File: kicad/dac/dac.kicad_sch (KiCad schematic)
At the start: 69 parts, among them J2 AudioJack3_SwitchT, J3 AudioJack3_SwitchTR, J3 Conn_01x09_Pin, J4 AudioJack3, K1 Relay, Q1 NPN, Q2 PNP, Q3 PNP, Q4 PNP, Q5 PNP, Q6 PNP, Q7 PNP, U1 PCM510xA

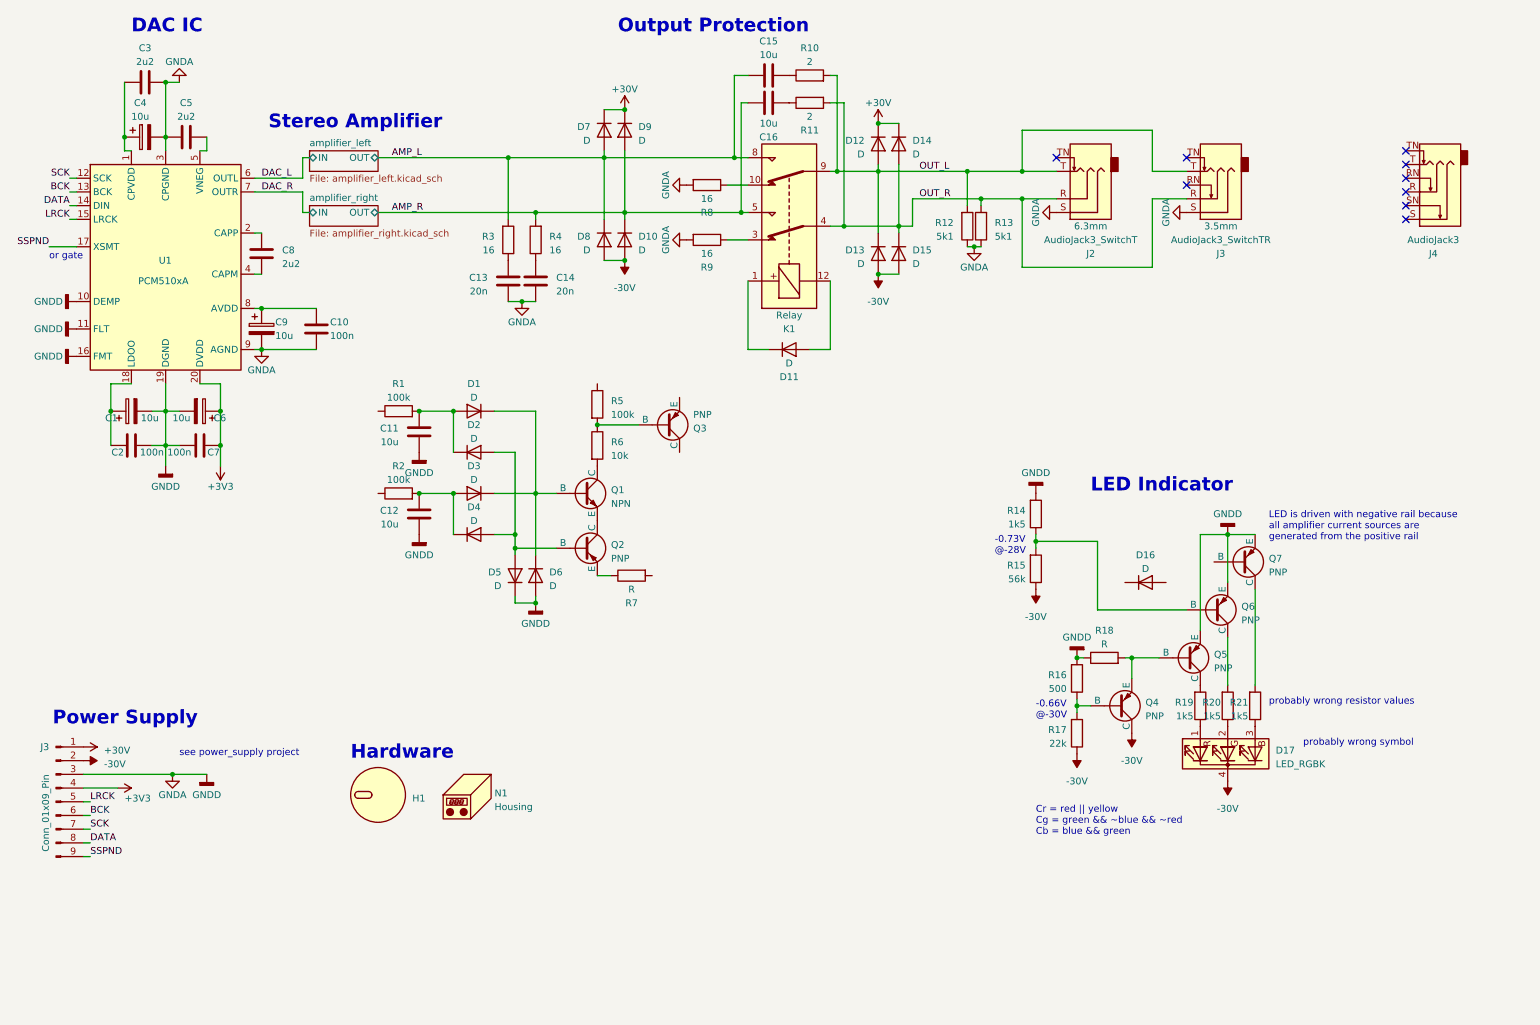
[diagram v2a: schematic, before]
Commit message: completed power supply footprints and placement
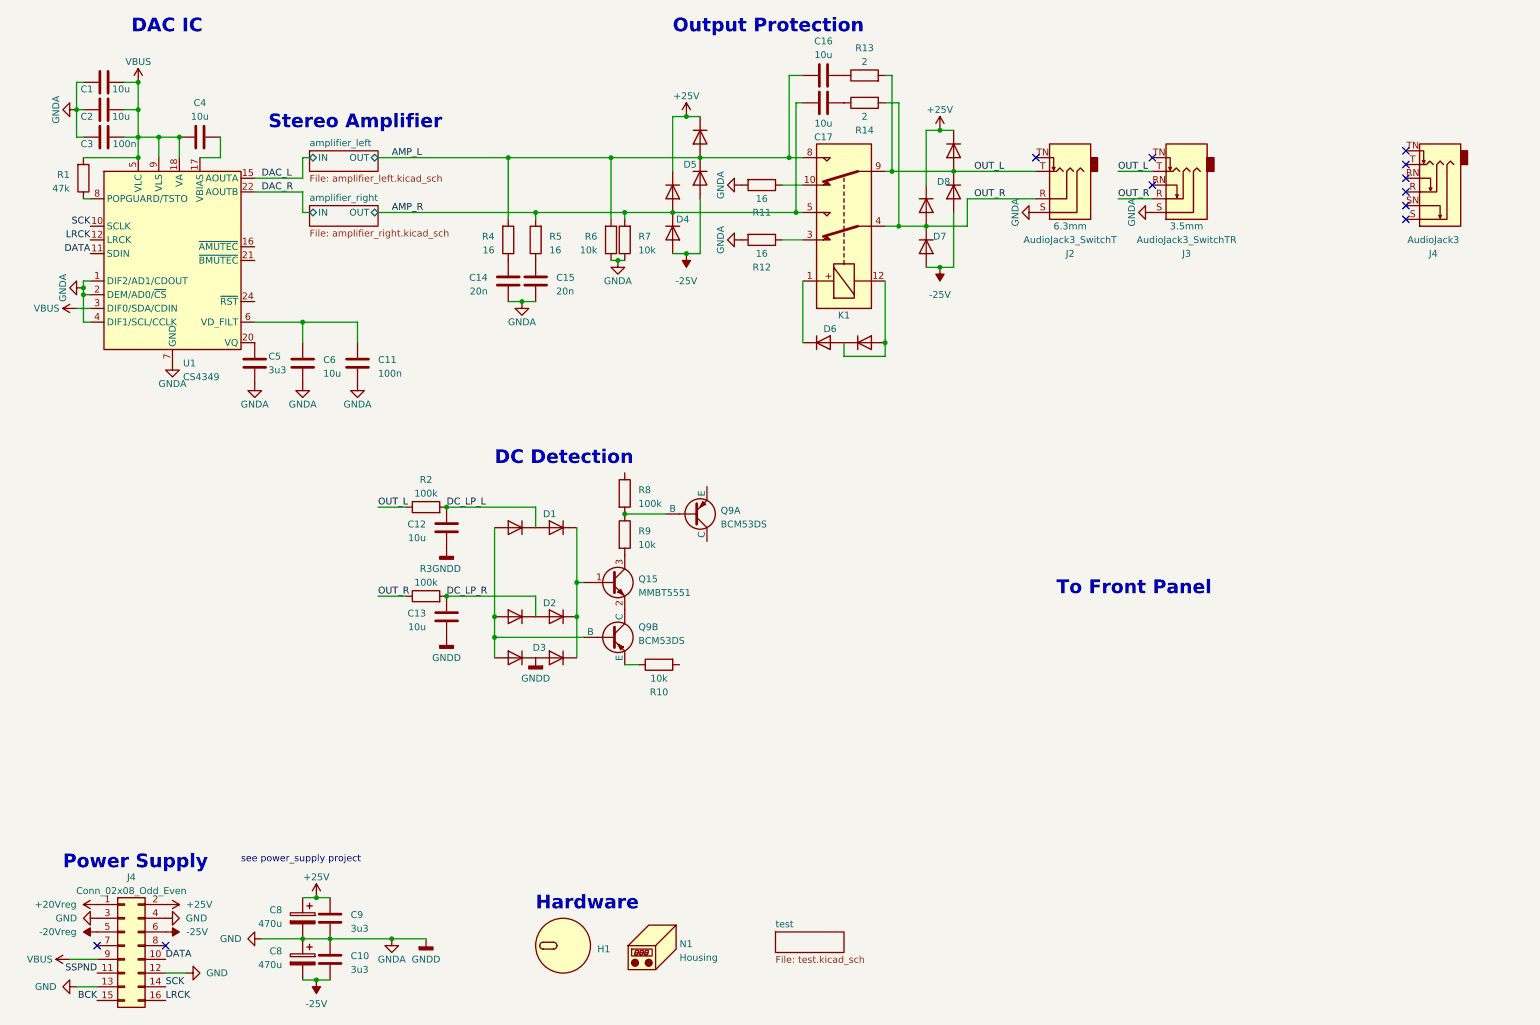
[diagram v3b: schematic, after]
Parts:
- removed C1, C4, C6, C9: 10u, symbol Device:C_Polarized
- removed C12: 10u, symbol Device:C
- removed C15: 10u, Capacitor_SMD:C_1206_3216Metric_Pad1.33x1.80mm_HandSolder, symbol Device:C
- removed C7: 100n, Capacitor_SMD:C_1206_3216Metric_Pad1.33x1.80mm_HandSolder, symbol Device:C
- removed C8: 2u2, Capacitor_SMD:C_1206_3216Metric_Pad1.33x1.80mm_HandSolder, symbol Device:C
- removed D1, D10, D11, D12, D13, D14, D15, D16, D2, D3, D4, D5, D6, D7, D8, D9: D, symbol Device:D
- removed D17: LED_RGBK, symbol Device:LED_RGBK
- removed J3: Conn_01x09_Pin, Connector_PinHeader_2.54mm:PinHeader_1x09_P2.54mm_Vertical, symbol Connector:Conn_01x09_Pin
- removed Q1: NPN, symbol Simulation_SPICE:NPN
- removed Q2, Q3: PNP, symbol Simulation_SPICE:PNP
- removed Q4, Q5, Q6, Q7: PNP, Package_TO_SOT_THT:TO-92, symbol Simulation_SPICE:PNP
- removed R14, R19, R20, R21: 1k5, Resistor_SMD:R_1206_3216Metric_Pad1.30x1.75mm_HandSolder, symbol Device:R
- removed R15: 56k, Resistor_SMD:R_1206_3216Metric_Pad1.30x1.75mm_HandSolder, symbol Device:R
- removed R16: 500, Resistor_SMD:R_1206_3216Metric_Pad1.30x1.75mm_HandSolder, symbol Device:R
- removed R17: 22k, Resistor_SMD:R_1206_3216Metric_Pad1.30x1.75mm_HandSolder, symbol Device:R
- removed R18: R, Resistor_SMD:R_1206_3216Metric_Pad1.30x1.75mm_HandSolder, symbol Device:R
- removed U1: PCM510xA, Package_SO:TSSOP-20_4.4x6.5mm_P0.65mm, symbol library:PCM510xA
- added C1, C13, C17, C4, C6: 10u, Capacitor_SMD:C_1206_3216Metric_Pad1.33x1.80mm_HandSolder, symbol Device:C
- added C11: 100n, Capacitor_SMD:C_1206_3216Metric_Pad1.33x1.80mm_HandSolder, symbol Device:C
- added C8 (x2): 470u, Capacitor_THT:CP_Radial_D10.0mm_P5.00mm, symbol Device:C_Polarized
- added C9: 3u3, Capacitor_THT:C_Rect_L7.2mm_W7.2mm_P5.00mm_FKS2_FKP2_MKS2_MKP2, symbol Device:C
- added D1, D2, D3, D4, D5, D6, D7, D8: ~, Package_TO_SOT_SMD:SOT-23-3, symbol library:Dual_Diode_Array
- added J4: Conn_02x08_Odd_Even, Connector_PinSocket_2.54mm:PinSocket_2x08_P2.54mm_Vertical, symbol Connector_Generic:Conn_02x08_Odd_Even
- added Q15: MMBT5551, Package_TO_SOT_SMD:SOT-23-3, symbol Device:Q_NPN_BEC
- added Q9: BCM53DS, Package_SO:SC-74-6_1.5x2.9mm_P0.95mm, symbol library:Dual-PNP
- added R1: 47k, Resistor_SMD:R_1206_3216Metric_Pad1.30x1.75mm_HandSolder, symbol Device:R
- added U1: CS4349, Package_SO:TSSOP-24_4.4x7.8mm_P0.65mm, symbol library:CS4349
- C10: value 100n -> 3u3; footprint Capacitor_SMD:C_1206_3216Metric_Pad1.33x1.80mm_HandSolder -> Capacitor_THT:C_Rect_L7.2mm_W7.2mm_P5.00mm_FKS2_FKP2_MKS2_MKP2; Digikey (none) -> 1928-1645-ND; Height (none) -> 13mm
- C12: renamed from C11; footprint (none) -> Capacitor_SMD:C_1206_3216Metric_Pad1.33x1.80mm_HandSolder; Digikey (none) -> 1276-3100-1-ND
- C16: Digikey (none) -> 1276-3100-1-ND
- C2: value 100n -> 10u; Digikey (none) -> 1276-3100-1-ND
- C3: value 2u2 -> 100n
- C5: value 2u2 -> 3u3
- R10: renamed from R7; value R -> 10k; footprint (none) -> Resistor_SMD:R_1206_3216Metric_Pad1.30x1.75mm_HandSolder
- R2: renamed from R1; footprint (none) -> Resistor_SMD:R_1206_3216Metric_Pad1.30x1.75mm_HandSolder
- R3: renamed from R2; footprint (none) -> Resistor_SMD:R_1206_3216Metric_Pad1.30x1.75mm_HandSolder
- R6: renamed from R12; value 5k1 -> 10k
- R7: renamed from R13; value 5k1 -> 10k
- R8: renamed from R5; footprint (none) -> Resistor_SMD:R_1206_3216Metric_Pad1.30x1.75mm_HandSolder
- R9: renamed from R6; footprint (none) -> Resistor_SMD:R_1206_3216Metric_Pad1.30x1.75mm_HandSolder
- renumbered C13 to C14, C14 to C15, R8 to R11, R9 to R12, R10 to R13, R11 to R14, R3 to R4, R4 to R5
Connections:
- net AMP_L: now also C16.1, R6.2, D5.3 (C/A)
- net AMP_R: now also R7.2, C17.1, D4.3 (C/A); no longer C16.1
- net BCK: now also J4.15 (Pin_15)
- net DAC_L: now also U1.15 (AOUTA)
- net DAC_R: now also U1.22 (AOUTB)
- net DATA: now also J4.10 (Pin_10), U1.11 (SDIN)
- net LRCK: now also J4.16 (Pin_16), U1.12 (LRCK)
- net OUT_L: now also R2.1, D8.3 (C/A); no longer R6.2
- net OUT_R: now also R3.1, D7.3 (C/A); no longer R7.2
- net SCK: now also J4.14 (Pin_14), U1.10 (SCLK)
- net SSPND: now also J4.11 (Pin_11)
- net -25V: now reaches C10.1
- net -25V: now also C8.2, D4.1 (A), D5.1 (A), D7.1 (A), D8.1 (A), J4.6 (Pin_6)
- net DC_LP_L: now reaches C12.1, R2.2
- net DC_LP_L: now also D1.3 (C/A)
- net at R9.2: now also Q15.3 (C)
- net at R8.2, R9.1: now also Q9.1 (B)
- net at R10.1: now also Q9.4 (E)
- net VBUS: now reaches C3.1
- net VBUS: now also C2.2, C1.2, C4.1, J4.9 (Pin_9), R1.2, U1.18 (VA), U1.3 (DIF0/SDA/CDIN), U1.5 (VLC), U1.9 (VLS)
- net at K1.1: now also D6.2 (C)
- net at K1.12: now also D6.1 (A), D6.3 (C/A)
- net at R14.1: now also C17.2; no longer C16.2
- net GND: now reaches C5.2
- net GND: now also C10.2, C12.2, C14.1, C15.1, C2.1, C3.2, J2.S, J3.S, R11.2, R12.2, R6.1, R7.1, C1.1, C11.2, C13.2, C6.2, C8.1, C8.2, C9.1, D3.3 (C/A), J4.12 (Pin_12), J4.13 (Pin_13), J4.3 (Pin_3), J4.4 (Pin_4), U1.1 (DIF2/AD1/CDOUT), U1.19 (GND), U1.2 (DEM/AD0/~{CS}), U1.4 (DIF1/SCL/CCLK), U1.7 (GND)
- net DC_LP_R: now reaches R3.2
- net DC_LP_R: now also C13.1, D2.3 (C/A)
- net at R13.1: now also C16.2
- removed net GNDA: C10.2, C12.2, C14.1, C15.1, C2.1, C3.2, C5.1, J2.S, J3.S, R11.2, R12.2, R6.1, R7.1
- new net: C4.2, U1.17 (VBIAS)
- new net: C5.1, U1.20 (VQ)
- new net: C11.1, C6.1, U1.6 (VD_FILT)
- new net: R1.1, U1.8 (POPGUARD/TSTO)
- new net: D1.2 (C), D2.2 (C), D3.2 (C), Q15.1 (B)
- new net: Q15.2 (E), Q9.3 (C)
- new net: D1.1 (A), D2.1 (A), D3.1 (A), Q9.2 (B)
- new net +20Vreg: J4.1 (Pin_1)
- new net +25V: C8.1, C9.2, D4.2 (C), D5.2 (C), D7.2 (C), D8.2 (C), J4.2 (Pin_2)
- new net -20Vreg: J4.5 (Pin_5)
- no-connect marks 9 -> 11
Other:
- added sheet test (test.kicad_sch)
- note added: "DC Detection"
- note added: "To Front Panel"
- note removed: "-0.66V @-30V"
- note removed: "-0.73V @-28V"
- note removed: "Cr = red || yellow Cg = green && ~blue && ~red Cb = blue && green"
- note removed: "LED Indicator"
- note removed: "LED is driven with negative rail because all amplifier current sources are generated from the positive rail"
- note removed: "or gate"
- note removed: "probably wrong resistor values"
- note removed: "probably wrong symbol"
- company: (none) -> Author: Jona Heinke
- title: USB DAC & Headphone Amplifier -> DAC & Headphone Amplifier
- moved on the sheet: C12, H1, J2, J3, K1, N1, R10, R11, R12, R13, R14, R2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

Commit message: commit
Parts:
- removed C14, C15: 20n, Capacitor_SMD:C_1206_3216Metric_Pad1.33x1.80mm_HandSolder, symbol Device:C
- removed D1, D2, D3, D4, D5, D6, D7, D8: ~, Package_TO_SOT_SMD:SOT-23-3, symbol library:Dual_Diode_Array
- removed R11, R12, R4, R5: 16, Resistor_SMD:R_1206_3216Metric_Pad1.30x1.75mm_HandSolder, symbol Device:R
- added D7: D, Diode_SMD:D_SOD-323_HandSoldering, symbol Device:D
- added D9 (x5): ~, Package_TO_SOT_SMD:SOT-23-3, symbol Device:D_Dual_Series_ACK
- added J5: Conn_01x06, symbol Connector_Generic:Conn_01x06
- added R6, R7: 16, Resistor_SMD:R_1206_3216Metric_Pad1.30x1.75mm_HandSolder, symbol Device:R
- J3: renamed from J4; now not fitted; now left out of the parts list
- K1: footprint (none) -> Relay_SMD:Relay_DPDT_Omron_G6K-2F-Y
- renumbered C11 to C10, C6 to C11, C16 to C12, C17 to C13, C12 to C14, C13 to C15, C5 to C7, C9 to C8, C10 to C9, J3 to J4, R8 to R10, R9 to R11, R10 to R12, R6 to R2, R7 to R3, R2 to R4, R3 to R5, R13 to R8, R14 to R9
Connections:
- net +25V: now also D9.3 (K), D9.3 (K), J5.1 (Pin_1)
- net -25V: now also D9.1 (A), D9.1 (A), J5.2 (Pin_2)
- net DC_LP_L: now also D9.2 (common)
- net DC_LP_R: now also D9.2 (common)
- net GND: now also C1.2, C2.2, D9.2 (common), J5.3 (Pin_3), R6.1, R7.1; no longer C1.1, C2.1
- net OUT_L: now also D9.2 (common)
- net OUT_R: now also D9.2 (common)
- net VBUS: now also C1.1, C2.1, R1.1; no longer C1.2, C2.2, R1.2
- net VBIAS: now reaches C4.2, U1.17 (VBIAS)
- net VQ: now reaches C7.1, U1.20 (VQ)
- net VD_FILT: now reaches C10.1, C11.1, U1.6 (VD_FILT)
- net POPGUARD: now reaches U1.8 (POPGUARD/TSTO)
- net POPGUARD: now also R1.2; no longer R1.1
- net at Q15.1 (B): now also D9.3 (K), D9.3 (K), D9.3 (K)
- net PROT_ARC_R: now reaches C13.2, R9.1
- net RLY+: now reaches K1.1
- net RLY+: now also D7.1 (K)
- net RLY_NC_L: now reaches K1.10
- net RLY_NC_L: now also R6.2
- net RLY-: now reaches K1.12
- net RLY-: now also D7.2 (A)
- net RLY_NC_R: now reaches K1.3
- net RLY_NC_R: now also R7.2
- net at Q9.2 (B): now also D9.1 (A), D9.1 (A), D9.1 (A)
- net PROT_ARC_L: now reaches C12.2, R8.1
- no-connect marks 11 -> 14
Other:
- note added: "DC USB"
- note added: "Input Pin Header From Power Supply Board"
- note added: "Output Jacks"
- note added: "fix relay pinout"
- note removed: "Power Supply"
- moved on the sheet: C11, C12, C13, C14, C15, C4, C7, J2, J4, K1, Q15, Q9A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

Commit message: commit
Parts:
- removed D9 (x3): ~, Package_TO_SOT_SMD:SOT-23-3, symbol Device:D_Dual_Series_ACK
- removed J3: AudioJack3, symbol Connector_Audio:AudioJack3_Switch
- removed Q15: MMBT5551, Package_TO_SOT_SMD:SOT-23-3, symbol Device:Q_NPN_BEC
- removed Q9: BCM53DS, Package_SO:SC-74-6_1.5x2.9mm_P0.95mm, symbol library:Dual-PNP
- removed R12: 10k, Resistor_SMD:R_1206_3216Metric_Pad1.30x1.75mm_HandSolder, symbol Device:R
- added C14: 3u3, Capacitor_SMD:C_1206_3216Metric_Pad1.33x1.80mm_HandSolder, symbol Device:C
- added D4, D5: TVS, Diode_SMD:D_SMB_Handsoldering, symbol Device:D_TVS
- added Q4: BCM53DS, Package_SO:SC-74-6_1.5x2.9mm_P0.95mm, symbol library:Dual-PNP
- added Q6: BCM56DS, Package_SO:SC-74-6_1.5x2.9mm_P0.95mm, symbol library:Dual-NPN
- added R4, R5, R8: 27k, Resistor_SMD:R_1206_3216Metric_Pad1.30x1.75mm_HandSolder, symbol Device:R
- added R6, R7: 47k, Resistor_SMD:R_1206_3216Metric_Pad1.30x1.75mm_HandSolder, symbol Device:R
- renumbered C4 to C10, C7 to C11, C10 to C12, C11 to C13, C12 to C15, C13 to C16, C8 to C3, C9 to C4, C1 to C5, C2 to C6, C3 to C7, C14 to C8, C15 to C9, J5 to J2, J4 to J3, J2 to J4, R3 to R10, R10 to R11, R11 to R12, R6 to R13, R7 to R14, R8 to R15, R9 to R16, R4 to R2, R5 to R3, R2 to R9
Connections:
- net RLY- is gone; now on net GND: D7.2 (A), K1.12
- net +25V: now also R11.1, C14.1, Q4.4 (E2), R8.1
- net AMP_L: now also R2.1
- net AMP_R: now also R3.1
- net DC_LP_L: now also R4.1; no longer D9.2 (common)
- net DC_LP_R: now also R5.1; no longer D9.2 (common)
- net GND: now also D4.1 (A1), D5.1 (A1), Q4.6 (C1), Q6.4 (E2), Q6.5 (E1), R6.2, R7.2
- net OUT_L: now also D4.2 (A2); no longer R2.1
- net OUT_R: now also D5.2 (A2); no longer R3.1
- net RLY+: now also Q4.3 (C2)
- net at R11.2, R12.1: now also Q4.2 (B2)
- net at R12.2: now also C14.2, Q6.3 (C2)
- net DC_POS: now reaches D9.3 (K), D9.3 (K)
- net DC_POS: now also Q6.1 (B1)
- net DC_NEG: now reaches D9.1 (A), D9.1 (A)
- net DC_NEG: now also Q4.1 (B1)
- new net: Q4.5 (E1), Q6.2 (B2), Q6.6 (C1), R8.2
- new net DC_VD_L: D9.2 (common), R4.2, R6.1
- new net DC_VD_R: D9.2 (common), R5.2, R7.1
- no-connect marks 14 -> 8
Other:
- note added: "replace with dual TVS reverse voltage > V+"
- note added: "use AUX circuit from https://sound-au.com/project05b.htm http://codeperspectives.com/computer-design/npn-pnp-logic-gates/"
- note removed: "see power_supply project"
- moved on the sheet: C10, C11, C12, C13, C15, C16, C3, C4, C5, C6, C7, C8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
